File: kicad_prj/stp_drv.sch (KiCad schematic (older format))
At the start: 12 parts

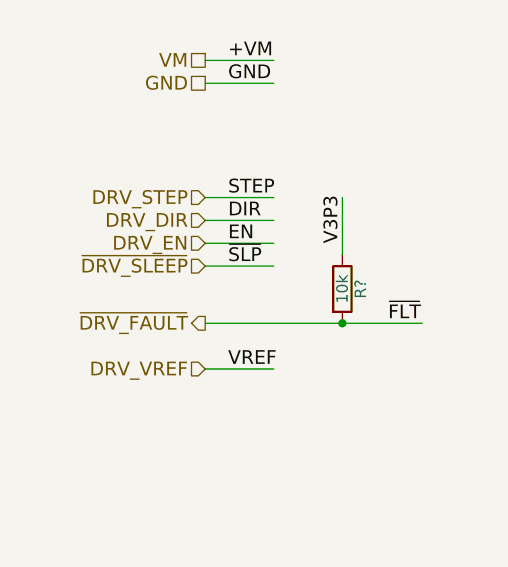
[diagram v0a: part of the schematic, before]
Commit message: Schematics 3
Added spindle driver and sensors/limit switches.
Need to add terminals for ADC channels.
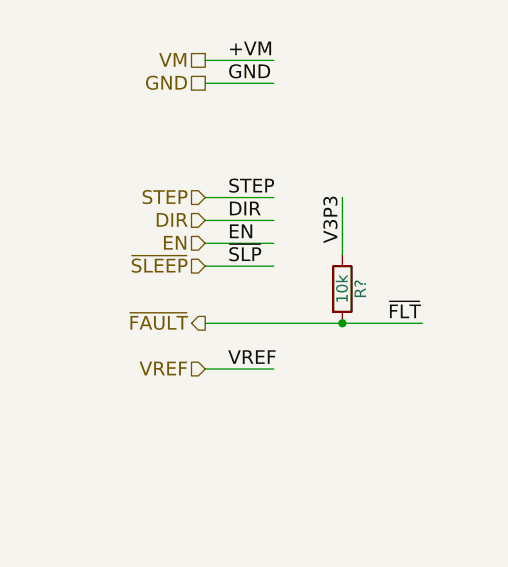
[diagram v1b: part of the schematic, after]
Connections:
- net labels added: ~FAULT, ~SLEEP
- net labels removed: DRV_DIR, DRV_EN, DRV_STEP, DRV_VREF, ~DRV_FAULT, ~DRV_SLEEP
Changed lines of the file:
@@
 $Descr A 11000 8500
 encoding utf-8
-Sheet 3 6
+Sheet 5 7
 Title "Stepper Driver"
 Date "2015-11-22"
@@
 AR Path="/56526EA5/56526EB2" Ref="U?"  Part="1"
 AR Path="/5653D417/56526EB2" Ref="U?"  Part="1"
+AR Path="/5654C1EE/56526EB2" Ref="U?"  Part="1"
 F 0 "U?" H 5300 3000 60  0000 C CNN
 F 1 "DRV8880" H 5450 3100 60  0000 C CNN
@@
 AR Path="/56526EA5/56526F71" Ref="P?"  Part="1"
 AR Path="/5653D417/56526F71" Ref="P?"  Part="1"
+AR Path="/5654C1EE/56526F71" Ref="P?"  Part="1"
 F 0 "P?" H 8150 2800 50  0000 C CNN
 F 1 "MX_01X04_SPRING" V 8250 2550 50  0000 C CNN
@@
 AR Path="/56526EA5/565270AE" Ref="R?"  Part="1"
 AR Path="/5653D417/565270AE" Ref="R?"  Part="1"
+AR Path="/5654C1EE/565270AE" Ref="R?"  Part="1"
 F 0 "R?" V 6980 4200 50  0000 C CNN
 F 1 "0.1" V 6900 4200 50  0000 C CNN
@@
 AR Path="/56526EA5/5652718B" Ref="R?"  Part="1"
 AR Path="/5653D417/5652718B" Ref="R?"  Part="1"
+AR Path="/5654C1EE/5652718B" Ref="R?"  Part="1"
 F 0 "R?" V 6980 4000 50  0000 C CNN
 F 1 "0.1" V 6900 4000 50  0000 C CNN
@@
 AR Path="/56526EA5/565273EE" Ref="C?"  Part="1"
 AR Path="/5653D417/565273EE" Ref="C?"  Part="1"
+AR Path="/5654C1EE/565273EE" Ref="C?"  Part="1"
 F 0 "C?" H 5325 2850 50  0000 L CNN
 F 1 "0.47uF" H 5325 2650 50  0000 L CNN
@@
 AR Path="/56526EA5/56527B5A" Ref="C?"  Part="1"
 AR Path="/5653D417/56527B5A" Ref="C?"  Part="1"
+AR Path="/5654C1EE/56527B5A" Ref="C?"  Part="1"
 F 0 "C?" H 5925 2850 50  0000 L CNN
 F 1 "0.47uF" H 5925 2650 50  0000 L CNN
@@
 AR Path="/56526EA5/56527B86" Ref="C?"  Part="1"
 AR Path="/5653D417/56527B86" Ref="C?"  Part="1"
+AR Path="/5654C1EE/56527B86" Ref="C?"  Part="1"
 F 0 "C?" H 6325 2850 50  0000 L CNN
 F 1 "0.1uF" H 6325 2650 50  0000 L CNN
@@
 AR Path="/56526EA5/56527BB1" Ref="C?"  Part="1"
 AR Path="/5653D417/56527BB1" Ref="C?"  Part="1"
+AR Path="/5654C1EE/56527BB1" Ref="C?"  Part="1"
 F 0 "C?" H 4825 2850 50  0000 L CNN
 F 1 "0.1uF" H 4825 2650 50  0000 L CNN
@@
 AR Path="/56526EA5/56527EEA" Ref="C?"  Part="1"
 AR Path="/5653D417/56527EEA" Ref="C?"  Part="1"
+AR Path="/5654C1EE/56527EEA" Ref="C?"  Part="1"
 F 0 "C?" H 5075 2850 50  0000 L CNN
 F 1 "0.1uF" H 5075 2650 50  0000 L CNN
@@
 AR Path="/56526EA5/565280CA" Ref="C?"  Part="1"
 AR Path="/5653D417/565280CA" Ref="C?"  Part="1"
+AR Path="/5654C1EE/565280CA" Ref="C?"  Part="1"
 F 0 "C?" H 4525 2850 50  0000 L CNN
 F 1 "220uF" H 4525 2650 50  0000 L CNN
@@
 AR Path="/56526EA5/5652A0D1" Ref="#PWR?"  Part="1"
 AR Path="/5653D417/5652A0D1" Ref="#PWR?"  Part="1"
+AR Path="/5654C1EE/5652A0D1" Ref="#PWR?"  Part="1"
 F 0 "#PWR?" H 4300 2850 50  0001 C CNN
 F 1 "GNDA" H 4300 2950 50  0000 C CNN
@@
 AR Path="/56526EA5/5652AD3D" Ref="#PWR?"  Part="1"
 AR Path="/5653D417/5652AD3D" Ref="#PWR?"  Part="1"
+AR Path="/5654C1EE/5652AD3D" Ref="#PWR?"  Part="1"
 F 0 "#PWR?" H 7100 4050 50  0001 C CNN
 F 1 "GNDA" H 7100 4150 50  0000 C CNN
@@
 AR Path="/56526EA5/5652CBA3" Ref="#PWR?"  Part="1"
 AR Path="/5653D417/5652CBA3" Ref="#PWR?"  Part="1"
+AR Path="/5654C1EE/5652CBA3" Ref="#PWR?"  Part="1"
 F 0 "#PWR?" H 6100 5000 50  0001 C CNN
 F 1 "GNDA" H 6100 5100 50  0000 C CNN
@@
 AR Path="/56526EA5/56530DCA" Ref="#PWR?"  Part="1"
 AR Path="/5653D417/56530DCA" Ref="#PWR?"  Part="1"
+AR Path="/5654C1EE/56530DCA" Ref="#PWR?"  Part="1"
 F 0 "#PWR?" H 4800 4250 50  0001 C CNN
 F 1 "GNDD" H 4800 4350 50  0000 C CNN
@@
 AR Path="/56526EA5/565318DF" Ref="P?"  Part="1"
 AR Path="/5653D417/565318DF" Ref="P?"  Part="1"
+AR Path="/5654C1EE/565318DF" Ref="P?"  Part="1"
 F 0 "P?" H 7950 3500 50  0000 C CNN
 F 1 "JMPR_02X03" H 7950 3100 50  0000 C CNN
@@
 AR Path="/56526EA5/56533262" Ref="#PWR?"  Part="1"
 AR Path="/5653D417/56533262" Ref="#PWR?"  Part="1"
+AR Path="/5654C1EE/56533262" Ref="#PWR?"  Part="1"
 F 0 "#PWR?" H 8200 3400 50  0001 C CNN
 F 1 "GNDD" H 8200 3500 50  0000 C CNN
@@
 AR Path="/56526EA5/56534F8B" Ref="R?"  Part="1"
 AR Path="/5653D417/56534F8B" Ref="R?"  Part="1"
+AR Path="/5654C1EE/56534F8B" Ref="R?"  Part="1"
 F 0 "R?" V 3280 3400 50  0000 C CNN
 F 1 "10k" V 3200 3400 50  0000 C CNN
@@
 ~SLP
 Text HLabel 2600 3000 0    60   Input ~ 0
-DRV_STEP
+STEP
 Text HLabel 2600 3100 0    60   Input ~ 0
-DRV_DIR
+DIR
 Text HLabel 2600 3200 0    60   Input ~ 0
-DRV_EN
+EN
 Text HLabel 2600 3300 0    60   Input ~ 0
-~DRV_SLEEP
+~SLEEP
 Text HLabel 2600 3750 0    60   Input ~ 0
-DRV_VREF
+VREF
 Text HLabel 2600 3550 0    60   Output ~ 0
-~DRV_FAULT
+~FAULT
 Wire Wire Line
 	2600 3000 2900 3000
@@
 AR Path="/56526EA5/565469D2" Ref="#PWR?"  Part="1"
 AR Path="/5653D417/565469D2" Ref="#PWR?"  Part="1"
+AR Path="/5654C1EE/565469D2" Ref="#PWR?"  Part="1"
 F 0 "#PWR?" H 7700 5300 50  0001 C CNN
 F 1 "GNDD" H 7700 5400 50  0000 C CNN
@@
 U 1 1 56546E45
 P 8200 5550
+AR Path="/5654C1EE/56546E45" Ref="#PWR?"  Part="1"
+AR Path="/56526EA5/56546E45" Ref="#PWR?"  Part="1"
 F 0 "#PWR?" H 8200 5300 50  0001 C CNN
 F 1 "GNDA" H 8200 5400 50  0000 C CNN
